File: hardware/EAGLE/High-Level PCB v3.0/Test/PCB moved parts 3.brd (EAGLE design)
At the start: 100 x 80 mm, 58 parts, among them IC1 MCP2551, IC2 DS8921, IC3 DS8921, J1 Optical Mouse, J2 RaspπUart, J8 DB9 Plug, J9 CAN Output, U1 COMPASS, U2 LLSHIFTER, U3 GPS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

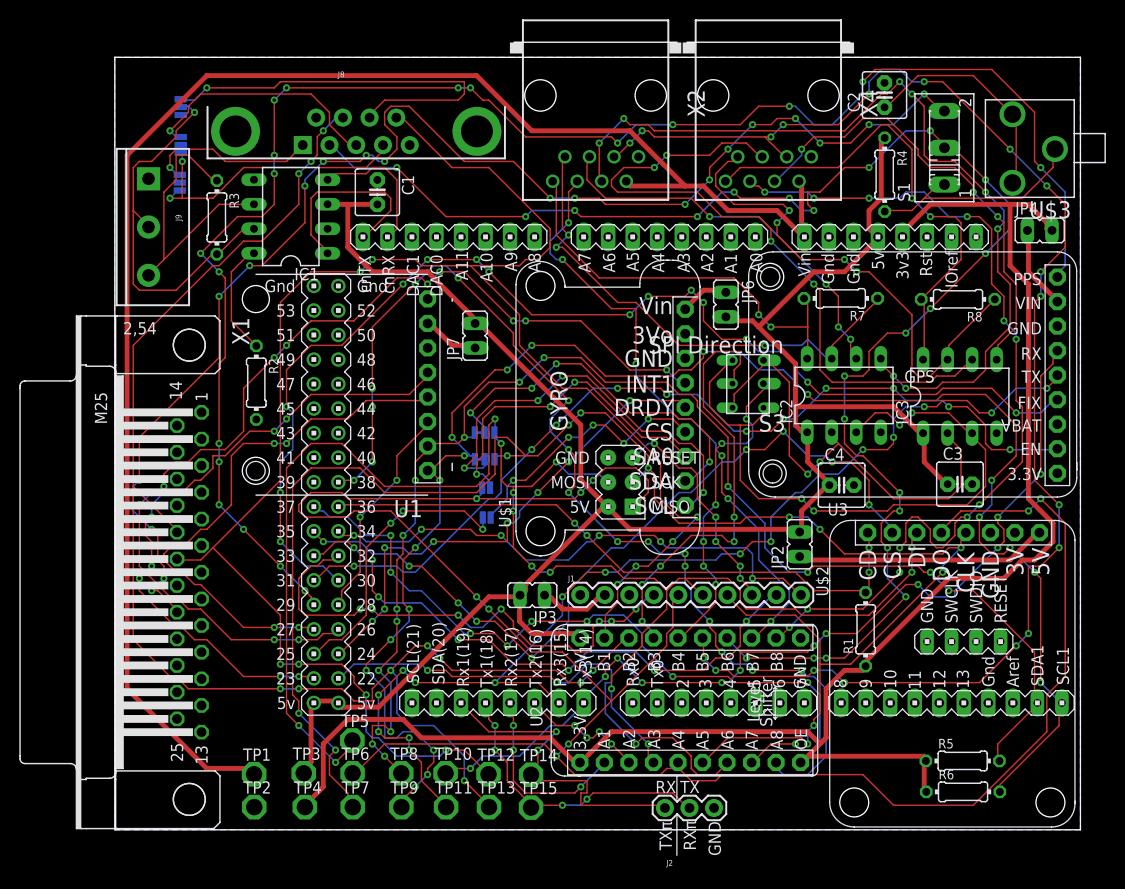
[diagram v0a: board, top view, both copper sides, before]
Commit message: The 3 board has no air wires!
And it has thick power traces.
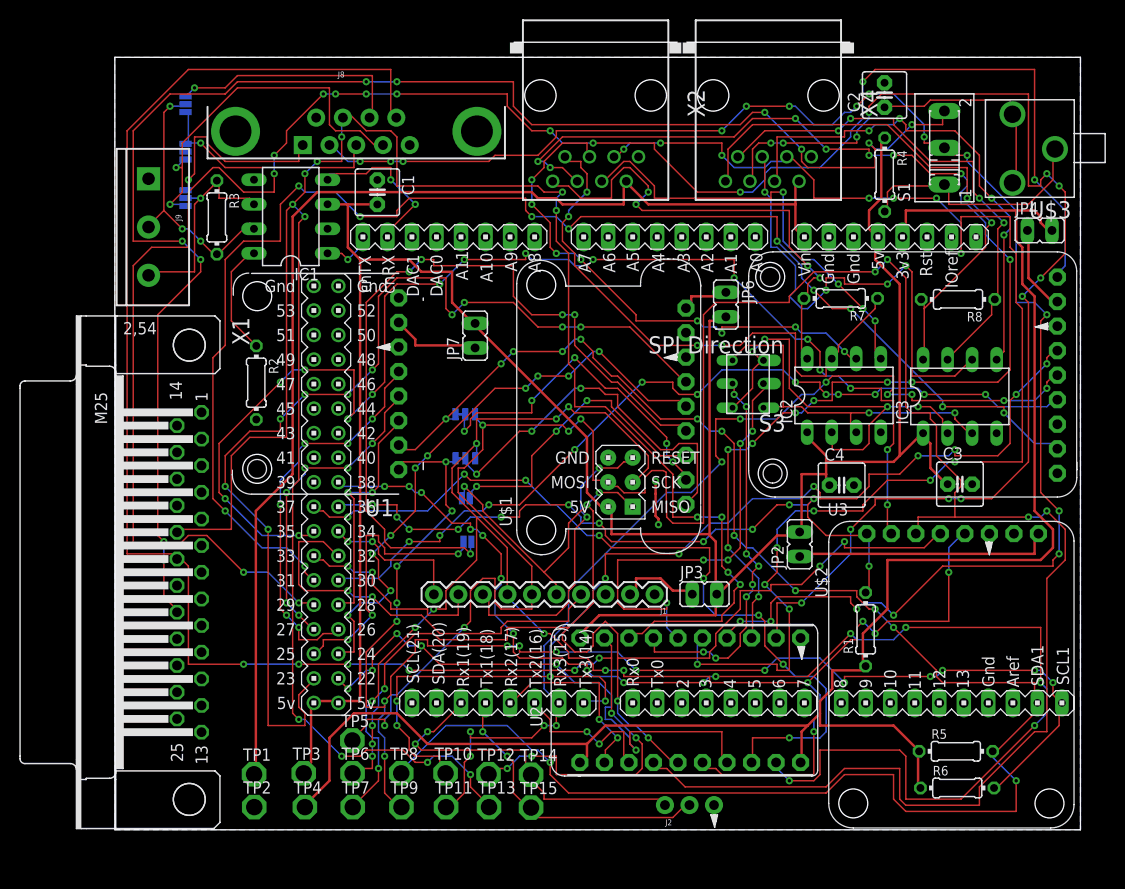
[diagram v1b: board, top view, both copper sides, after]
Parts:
- J2: device tx_rxRasp:1X03 -> ELCano_Footprints:1X03
- U1: device ELCOMPASS:ELCOMPASS -> ELCano_Footprints:ELCOMPASS
- U2: device ELSHIFTER:ELSHIFTER -> ELCano_Footprints:ELSHIFTER
- U3: device ELGPS:ELGPS -> ELCano_Footprints:ELGPS
- moved U$2 31.1 mm to (86.6, 0.20)
- moved JP3 17.8 mm to (61.1, 24.4), turned to 270 degrees
- moved U2 14.2 mm to (72.8, 12.2)
- moved U$1 9.97 mm to (51.7, 31.1)
- moved J1 7.70 mm to (55.9, 24.4), turned to 180 degrees
- moved JP5 3.20 mm to (36.5, 29.8)
- moved U1 3.00 mm to (30.7, 56.4)
- moved JP9 2.76 mm to (36.3, 43.0)
- moved JP1 2.37 mm to (36.4, 34.3)
- moved JP8 2.00 mm to (36.3, 38.5)
- moved JP10 1.71 mm to (7.33, 65.4)
- moved R5 1.22 mm to (87.1, 8.13)
- moved JP11 0.86 mm to (7.33, 70.2)
- moved R6 0.72 mm to (87.2, 4.33)
- moved JP12 0.58 mm to (7.33, 75.1)
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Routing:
- net MOSI: track 169.7 -> 259.6 mm, vias 13 -> 9
- net C2_RX: track 152.6 -> 235.0 mm, vias 11 -> 15
- net MISO: track 226.2 -> 149.9 mm, vias 9 -> 11
- net CS_C5_FRONT_5V: track 63.2 -> 131.5 mm, vias 6 -> 16
- net EN: track 93.9 -> 149.2 mm
- net N$19: track 27.6 -> 82.9 mm
- net CS_SD: track 83.2 -> 132.6 mm, vias 9 -> 16
- net MISO-: track 89.7 -> 45.0 mm, vias 8 -> 4
- net +5V: track 207.0 -> 251.5 mm
- net SDA1: track 141.9 -> 184.0 mm, vias 15 -> 13
- net VIN: track 164.5 -> 122.5 mm
- net NPD: track 61.8 -> 21.2 mm, vias 7 -> 2
- net LED: track 55.3 -> 15.1 mm, vias 6 -> 2
- net FIX: track 122.0 -> 88.4 mm, vias 14 -> 12
- net N$3: track 67.7 -> 37.9 mm, vias 4 -> 2
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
